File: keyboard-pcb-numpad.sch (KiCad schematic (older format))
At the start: 14 parts

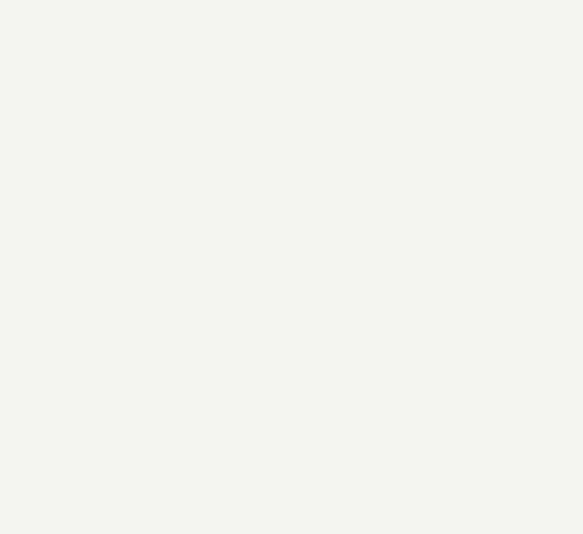
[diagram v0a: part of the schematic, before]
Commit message: init: add promicro lib
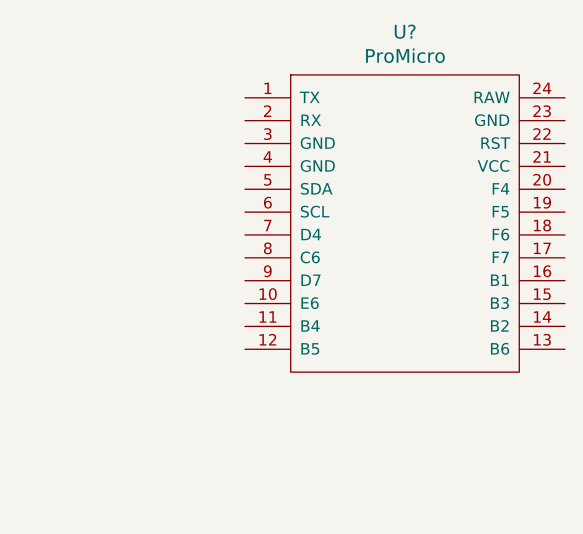
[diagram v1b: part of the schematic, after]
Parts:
- added U?: ProMicro, symbol promicro:ProMicro
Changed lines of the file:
@@
 Text GLabel 4100 3450 0    50   Input ~ 0
 D-
+$Comp
+L promicro:ProMicro U?
+U 1 1 616BD093
+P 8300 2550
+F 0 "U?" H 8300 3587 60  0000 C CNN
+F 1 "ProMicro" H 8300 3481 60  0000 C CNN
+F 2 "" H 8400 1500 60  0000 C CNN
+F 3 "" H 8400 1500 60  0000 C CNN
+	1    8300 2550
+	1    0    0    -1
+$EndComp
 $EndSCHEMATC

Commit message: feat: complete electrical setup
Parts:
- removed C?: 1uF, symbol Device:C_Small
- removed C? (x3): 0.1uF, symbol Device:C_Small
- removed C?: 10uF, symbol Device:C_Small
- removed C? (x2): 22pF, symbol Device:C_Small
- removed R? (x2): 10k, symbol Device:R_Small
- removed R? (x2): 22, symbol Device:R_Small
- removed SW?: SW_Push, symbol Switch:SW_Push
- removed U?: ATmega32U4-AU, Package_QFP:TQFP-44_10x10mm_P0.8mm, symbol MCU_Microchip_ATmega:ATmega32U4-AU
- removed Y?: 16MHz, symbol Device:Crystal_GND24_Small
- added D? (x17): D_Small, symbol Device:D_Small
- added MX? (x17): MX-NoLED, symbol MX_Alps_Hybrid:MX-NoLED
- added R?: R_Small, symbol Device:R_Small
- added SW?: SW_Push, symbol Switch:SW_Push
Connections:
- net +5V: now also U?.21 (VCC), R?.2
- net GND: now also U?.23 (GND), U?.3 (GND), U?.4 (GND), SW?.1
- net ROW2: now reaches U?.10 (E6)
- net ROW2: now also D?.1 (K), D?.1 (K), D?.1 (K), D?.1 (K)
- net ROW3: now reaches U?.11 (B4)
- net ROW3: now also D?.1 (K), D?.1 (K), D?.1 (K)
- net ROW4: now reaches U?.12 (B5)
- net ROW4: now also D?.1 (K), D?.1 (K), D?.1 (K)
- net COL3: now reaches U?.15 (B3)
- net COL3: now also MX?.1 (COL), MX?.1 (COL), MX?.1 (COL)
- net COL2: now reaches U?.16 (B1)
- net COL2: now also MX?.1 (COL), MX?.1 (COL), MX?.1 (COL), MX?.1 (COL), MX?.1 (COL)
- net COL1: now reaches U?.17 (F7)
- net COL1: now also MX?.1 (COL), MX?.1 (COL), MX?.1 (COL), MX?.1 (COL), MX?.1 (COL)
- net COL0: now reaches U?.18 (F6)
- net COL0: now also MX?.1 (COL), MX?.1 (COL), MX?.1 (COL), MX?.1 (COL)
- net RST: now reaches U?.22 (RST)
- net RST: now also R?.1, SW?.2
- net ROW0: now reaches U?.8 (C6)
- net ROW0: now also D?.1 (K), D?.1 (K), D?.1 (K), D?.1 (K)
- net ROW1: now reaches U?.9 (D7)
- net ROW1: now also D?.1 (K), D?.1 (K), D?.1 (K)
- new net: D?.2 (A), MX?.2 (ROW) (x17)
- no-connect marks 0 -> 10
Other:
- moved on the sheet: U?
